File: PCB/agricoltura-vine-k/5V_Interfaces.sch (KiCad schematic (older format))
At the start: 26 parts, among them K1 G5LE-14_DC5, K2 G5LE-14_DC5, Q1 IRLML6346TRPBF, Q2 IRLML6346TRPBF, T19 TSW-108-07-G-T, T20 0010897080, T22 0395121006, U10 ZXGD3009E6TA, U8 TCA6416ARTWR, U9 ZXGD3009E6TA

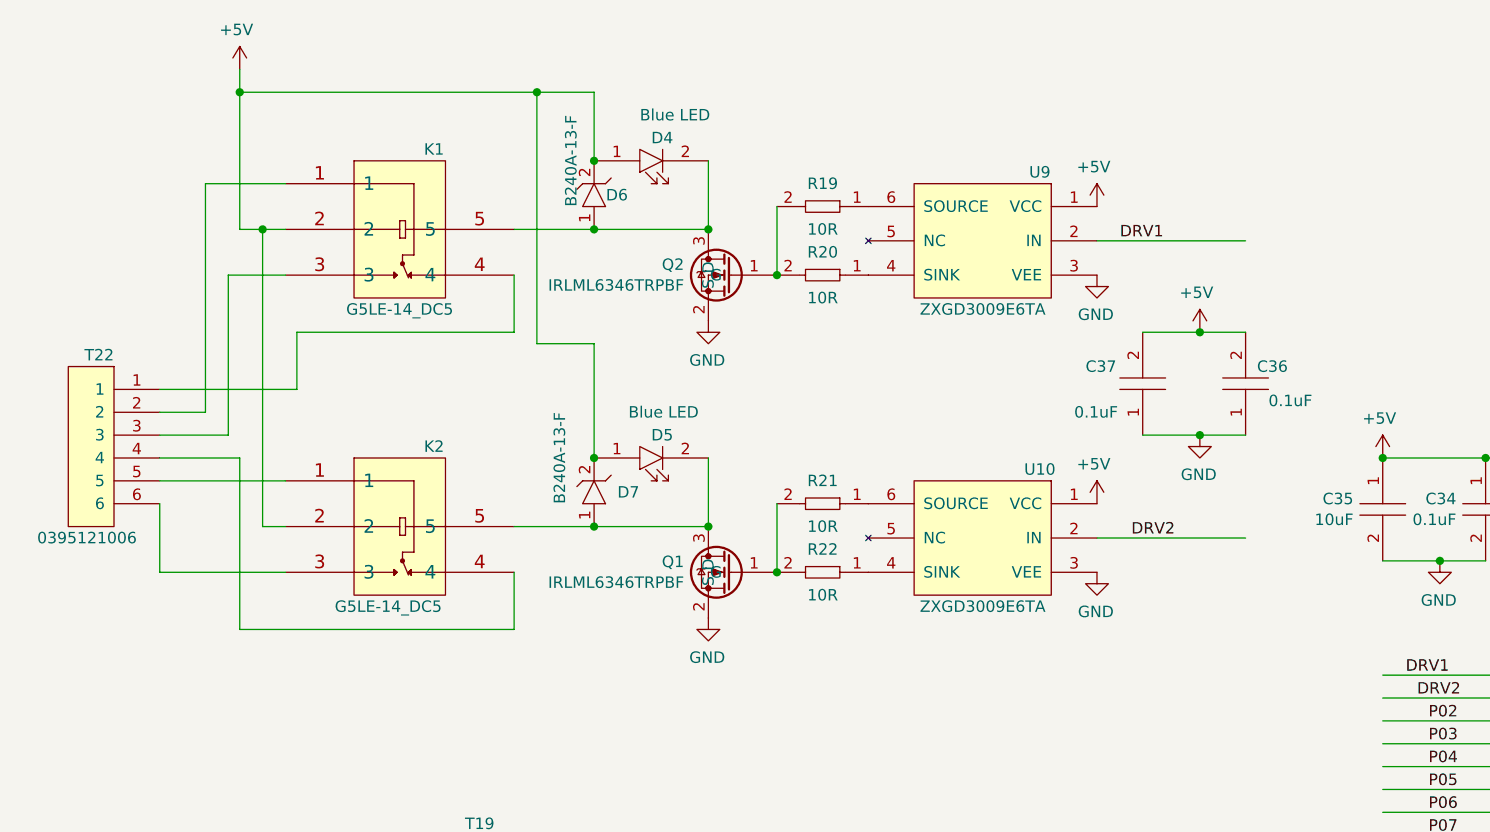
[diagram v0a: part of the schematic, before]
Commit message: Relay and Board
Relay circuits added and exported to PCB
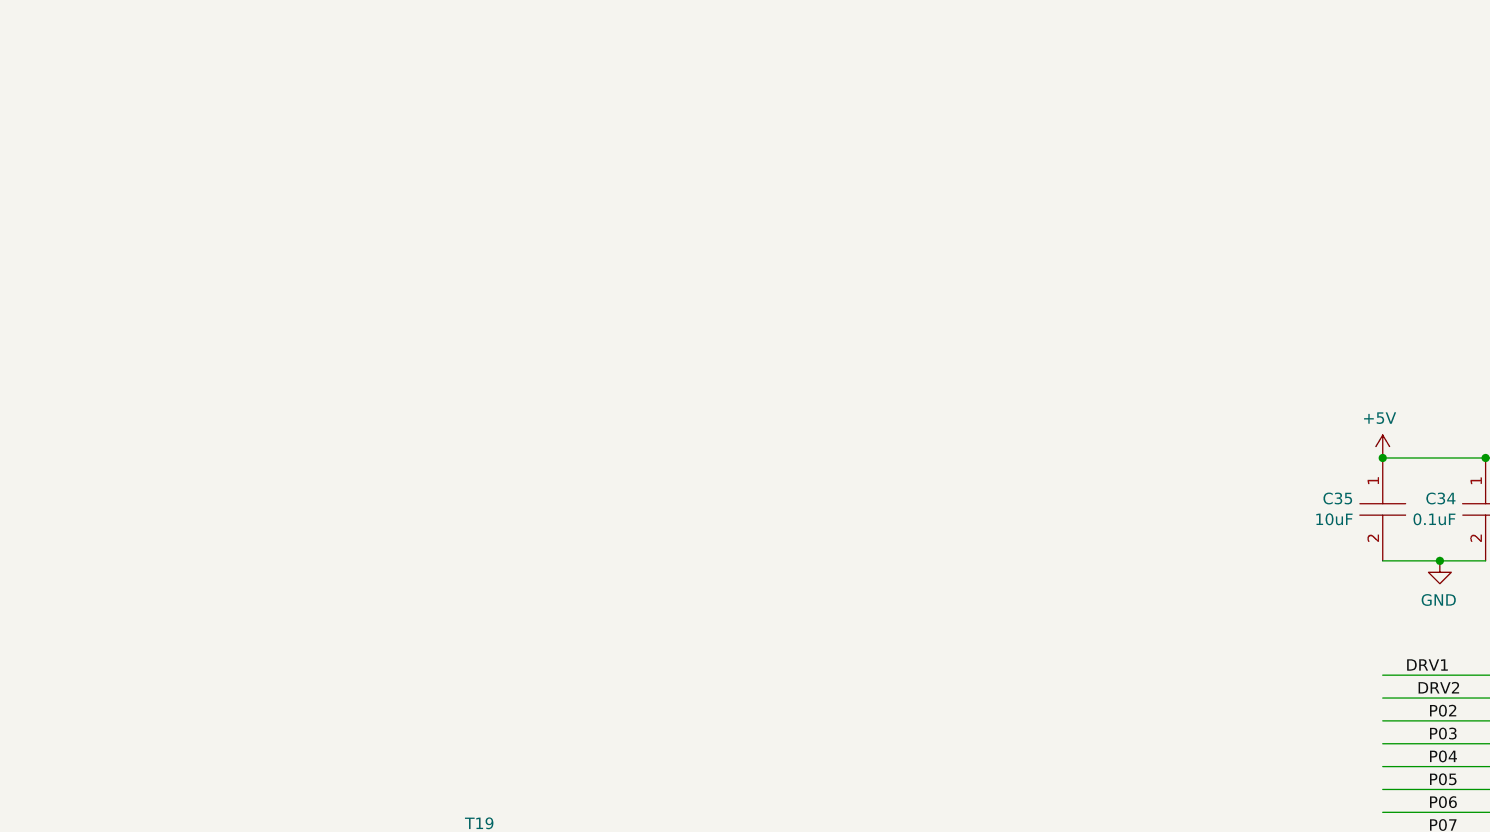
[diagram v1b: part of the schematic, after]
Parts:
- removed C36, C37: C0402C104K9PACTU, AVR-KiCAD-Lib-Resistors:R0402, symbol AVR-KiCAD-Lib-Capacitors:C0402C104K9PACTU
- removed D4, D5: LTST-C194TBKT, AVR-KiCAD-Lib-Diodes:LED0603, symbol AVR-KiCAD-Lib-Diodes:LTST-C194TBKT
- removed D6, D7: B240A-13-F, AVR-KiCAD-Lib-Diodes:B240A-13-F, symbol AVR-KiCAD-Lib-Diodes:B240A-13-F
- removed K1, K2: G5LE-14_DC5, AVR-KiCAD-Lib-Relays-Contactors:G5LE-14_DC5, symbol AVR-KiCAD-Lib-Mech-Relays-Contactors:G5LE-14_DC5
- removed Q1, Q2: IRLML6346TRPBF, AVR-KiCAD-Lib-Transistors:SOT-23, symbol AVR-KiCAD-Lib-Transistors:IRLML6346TRPBF
- removed R19, R20, R21, R22: RC0402FR-0710RL, AVR-KiCAD-Lib-Resistors:R0402, symbol AVR-KiCAD-Lib-Diodes:RC0402FR-0710RL
- removed T22: 0395121006, AVR-KiCAD-Lib-Connectors:0395121006, symbol AVR-KiCAD-Lib-Connectors:0395121006
- removed U10, U9: ZXGD3009E6TA, growbox-KiCAD-ICs:SOT-23-6_Handsoldering, symbol AVR-KiCAD-Lib-ICs:ZXGD3009E6TA
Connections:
- wire segments 106 -> 63

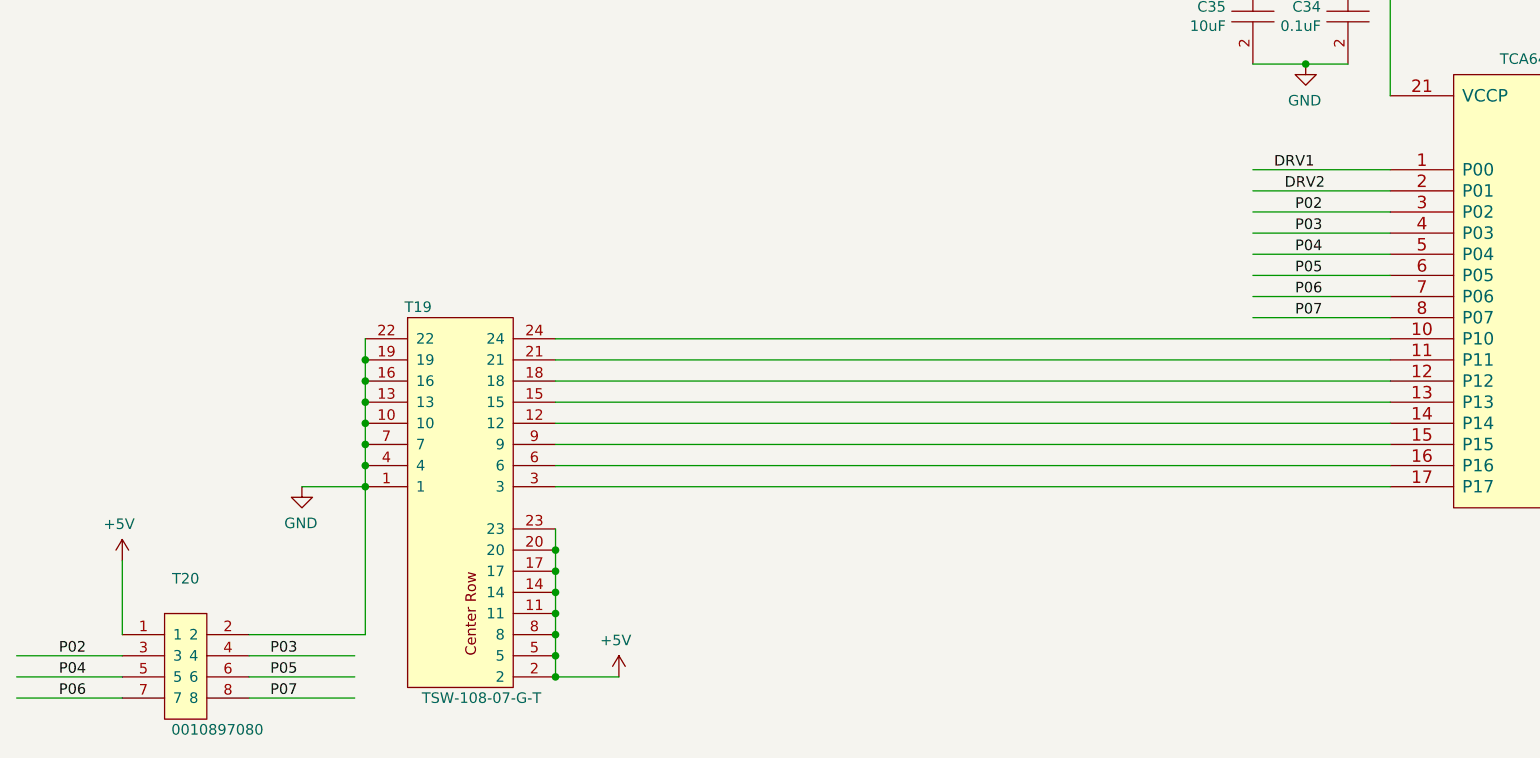
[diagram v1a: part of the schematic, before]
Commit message: Finished
PCB routing complete, up for review before fab.
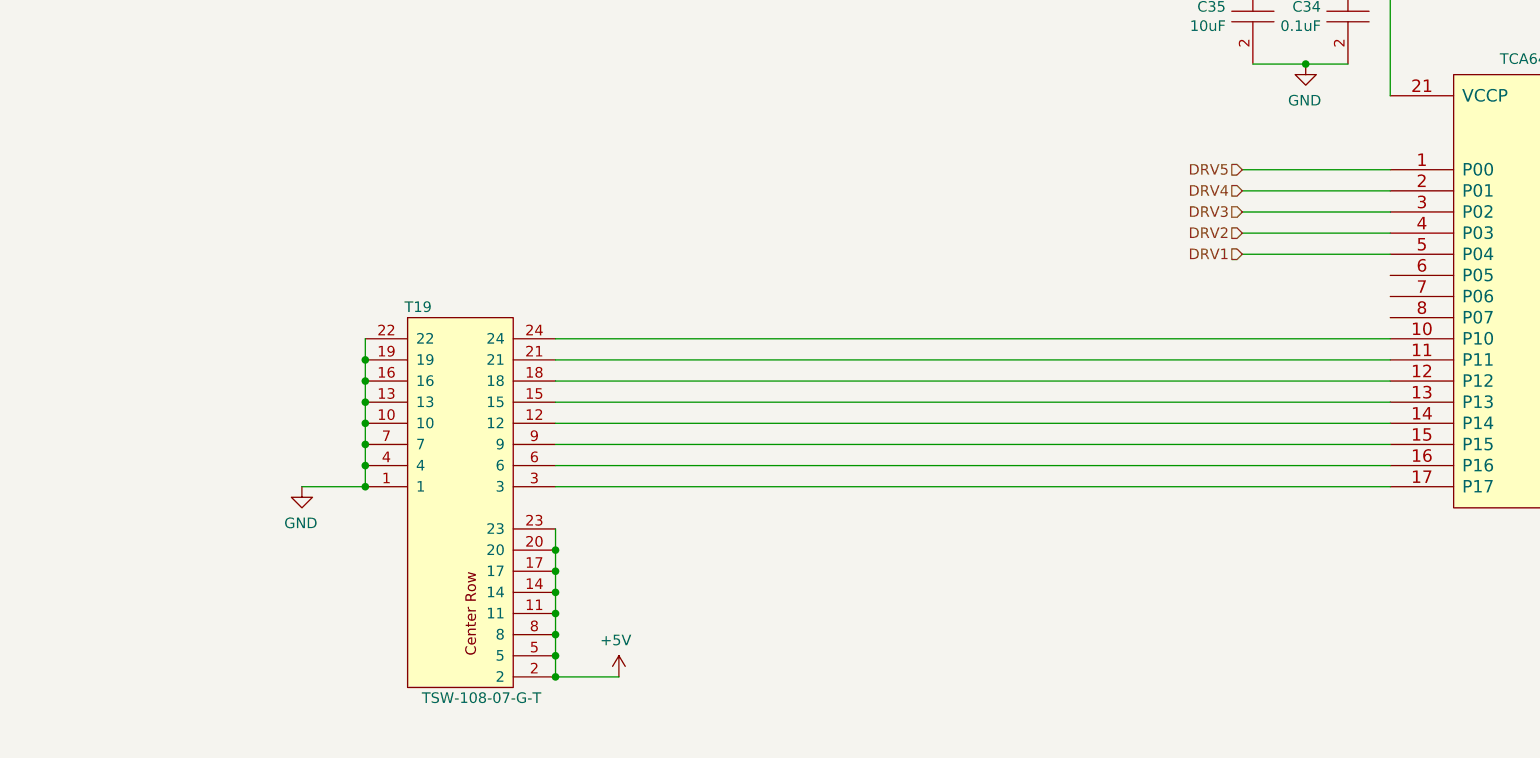
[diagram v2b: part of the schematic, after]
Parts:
- removed T20: 0010897080, AVR-KiCAD-Lib-Connectors:Pin_Header_Straight_2x04_Pitch2.54mm, symbol AVR-KiCAD-Lib-Connectors:0010897080
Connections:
- net labels added: DRV3, DRV4, DRV5
- net labels removed: P02, P03, P04, P05, P06, P07
- wire segments 63 -> 51
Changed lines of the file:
@@
 $EndDescr
-$Comp
-L AVR-KiCAD-Lib-Connectors:TSW-108-07-G-T T19
-U 1 1 5F0EF8CA
-P 2800 5200
-F 0 "T19" H 2850 5250 50  0000 C CNN
-F 1 "TSW-108-07-G-T" H 3150 3400 50  0000 C CNN
-F 2 "AVR-KiCAD-Lib-Connectors:TSW-108-07-G-T" H 2600 5200 50  0001 C CNN
-F 3 "http://suddendocs.samtec.com/catalog_english/tsw_th.pdf" H 2700 5300 50  0001 C CNN
-F 4 "2.51000" H 2900 5450 50  0001 C CNN "Cost QTY: 1"
-F 5 "1.39350" H 3000 5550 50  0001 C CNN "Cost QTY: 1000"
-F 6 "*" H 3100 5650 50  0001 C CNN "Cost QTY: 2500"
-F 7 "1.23557" H 3200 5750 50  0001 C CNN "Cost QTY: 5000"
-F 8 "1.20770" H 3300 5850 50  0001 C CNN "Cost QTY: 10000"
-F 9 "Samtec Inc." H 3400 5950 50  0001 C CNN "MFR"
-F 10 "TSW-108-07-G-T" H 3500 6050 50  0001 C CNN "MFR#"
-F 11 "Digikey" H 3600 6150 50  0001 C CNN "Vendor"
-F 12 "SAM10855-ND" H 3700 6250 50  0001 C CNN "Vendor #"
-F 13 "AVR" H 3800 6350 50  0001 C CNN "Designer"
-F 14 "10.92mm" H 3900 6450 50  0001 C CNN "Height"
-F 15 "6/18/2020" H 5000 7550 50  0001 C CNN "Date Created"
-F 16 "6/18/2020" H 4000 6550 50  0001 C CNN "Date Modified"
-F 17 "Yes" H 4100 6650 50  0001 C CNN "Lead-Free ?"
-F 18 "1" H 4200 6750 50  0001 C CNN "RoHS Levels"
-F 19 "SMT" H 4300 6850 50  0001 C CNN "Mounting"
-F 20 "24" H 4400 6950 50  0001 C CNN "Pin Count #"
-F 21 "Active" H 4500 7050 50  0001 C CNN "Status"
-F 22 "*" H 4600 7150 50  0001 C CNN "Tolerance"
-F 23 "Connector" H 4700 7250 50  0001 C CNN "Type"
-F 24 "*" H 4800 7350 50  0001 C CNN "Voltage"
-F 25 "*" H 4900 7500 50  0001 C CNN "Package"
-F 26 "Connector Header Through Hole 24 position 0.100\" (2.54mm)" H 5300 7900 50  0001 C CNN "Description"
-F 27 "3X08" H 5100 7700 50  0001 C CNN "_Value_"
-F 28 "*" H 5200 7800 50  0001 C CNN "Management_ID"
-	1    2800 5200
-	1    0    0    -1
-$EndComp
 $Comp
 L power:GND #PWR061
@@
 Connection ~ 10500 3900
 Wire Wire Line
+	7450 5300 3500 5300
+Wire Wire Line
+	7450 5400 3500 5400
+Wire Wire Line
+	7450 5500 3500 5500
+Wire Wire Line
+	7450 5600 3500 5600
+Wire Wire Line
+	7450 5700 3500 5700
+Wire Wire Line
+	7450 5800 3500 5800
+Wire Wire Line
+	7450 5900 3500 5900
+Wire Wire Line
+	7450 6000 3500 6000
+Connection ~ 10500 4700
+Connection ~ 10150 4800
+Wire Wire Line
+	10750 4700 10500 4700
+Wire Wire Line
+	10750 4800 10150 4800
+Connection ~ 7050 4000
+Text HLabel 6750 4600 0    50   Input ~ 0
+DRV4
+Text HLabel 6750 4700 0    50   Input ~ 0
+DRV3
+Text HLabel 6750 4800 0    50   Input ~ 0
+DRV2
+Text HLabel 6750 4900 0    50   Input ~ 0
+DRV1
+Text HLabel 6750 4500 0    50   Input ~ 0
+DRV5
+Connection ~ 2600 6000
+Connection ~ 3500 6700
+Connection ~ 2600 5800
+Wire Wire Line
+	3500 6700 3500 6800
+Wire Wire Line
+	3500 6800 3500 6900
+Connection ~ 3500 6800
+Wire Wire Line
+	2600 5900 2600 6000
+Wire Wire Line
+	2600 5800 2600 5900
+Connection ~ 2600 5900
+Wire Wire Line
 	3500 6200 3500 6300
-Wire Wire Line
-	7450 5300 3500 5300
-Wire Wire Line
-	7450 5400 3500 5400
-Wire Wire Line
-	7450 5500 3500 5500
-Wire Wire Line
-	7450 5600 3500 5600
-Wire Wire Line
-	7450 5700 3500 5700
-Wire Wire Line
-	7450 5800 3500 5800
-Wire Wire Line
-	7450 5900 3500 5900
-Wire Wire Line
-	7450 6000 3500 6000
+Connection ~ 3500 6300
 Connection ~ 3500 6900
-Connection ~ 3500 6800
-Wire Wire Line
-	3500 6800 3500 6900
-Connection ~ 3500 6700
-Wire Wire Line
-	3500 6700 3500 6800
-Connection ~ 3500 6600
-Wire Wire Line
-	3500 6600 3500 6700
+Wire Wire Line
+	2600 5300 2600 5400
+Connection ~ 2600 5400
+Wire Wire Line
+	3500 6300 3500 6400
+Connection ~ 3500 6400
+Wire Wire Line
+	2600 5400 2600 5500
+Connection ~ 2600 5500
+Wire Wire Line
+	3500 6400 3500 6500
 Connection ~ 3500 6500
-Wire Wire Line
-	3500 6500 3500 6600
-Connection ~ 3500 6400
-Wire Wire Line
-	3500 6400 3500 6500
-Connection ~ 3500 6300
-Wire Wire Line
-	3500 6300 3500 6400
-Wire Wire Line
-	2600 5300 2600 5400
-Wire Wire Line
-	2600 5400 2600 5500
-Connection ~ 2600 5400
-Connection ~ 2600 6000
-Connection ~ 2600 5500
 Wire Wire Line
 	2600 5500 2600 5600
 Connection ~ 2600 5600
 Wire Wire Line
+	3500 6500 3500 6600
+Wire Wire Line
+	3500 6600 3500 6700
+Connection ~ 3500 6600
+Wire Wire Line
+	2600 5700 2600 5800
+Wire Wire Line
 	2600 5600 2600 5700
 Connection ~ 2600 5700
-Wire Wire Line
-	2600 5700 2600 5800
-Connection ~ 2600 5800
-Wire Wire Line
-	2600 5800 2600 5900
-Connection ~ 2600 5900
-Wire Wire Line
-	2600 5900 2600 6000
-Connection ~ 10500 4700
-Connection ~ 10150 4800
-Wire Wire Line
-	10750 4700 10500 4700
-Wire Wire Line
-	10750 4800 10150 4800
-Connection ~ 7050 4000
-Wire Wire Line
-	6800 4500 7450 4500
-Text Label 6900 4500 0    50   ~ 0
-DRV1
-$Comp
-L AVR-KiCAD-Lib-Connectors:0010897080 T20
-U 1 1 5EFE35FE
-P 1650 6600
-F 0 "T20" H 1750 6765 50  0000 C CNN
-F 1 "0010897080" H 1900 6050 50  0000 C CNN
-F 2 "AVR-KiCAD-Lib-Connectors:Pin_Header_Straight_2x04_Pitch2.54mm" H 1450 6550 50  0001 C CNN
-F 3 "https://www.molex.com/pdm_docs/sd/010897080_sd.pdf" H 1550 6700 50  0001 C CNN
-F 4 "1.05000" H 1750 6850 50  0001 C CNN "Cost QTY: 1"
-F 5 "0.57952" H 1850 6950 50  0001 C CNN "Cost QTY: 1000"
-F 6 "*" H 1950 7050 50  0001 C CNN "Cost QTY: 2500"
-F 7 "0.50708" H 2050 7150 50  0001 C CNN "Cost QTY: 5000"
-F 8 "0.48173" H 2150 7250 50  0001 C CNN "Cost QTY: 10000"
-F 9 "Molex" H 2250 7350 50  0001 C CNN "MFR"
-F 10 "0010897080" H 2350 7450 50  0001 C CNN "MFR#"
-F 11 "Digikey" H 2450 7550 50  0001 C CNN "Vendor"
-F 12 "0010897080" H 2550 7650 50  0001 C CNN "Vendor #"
-F 13 "AVR" H 2650 7750 50  0001 C CNN "Designer"
-F 14 "8.4mm" H 2750 7850 50  0001 C CNN "Height"
-F 15 "6/30/2020" H 3850 8950 50  0001 C CNN "Date Created"
-F 16 "6/30/2020" H 2850 7950 50  0001 C CNN "Date Modified"
-F 17 "Yes" H 2950 8050 50  0001 C CNN "Lead-Free ?"
-F 18 "1" H 3050 8150 50  0001 C CNN "RoHS Levels"
-F 19 "ThroughHole" H 3150 8250 50  0001 C CNN "Mounting"
-F 20 "8" H 3250 8350 50  0001 C CNN "Pin Count #"
-F 21 "Active" H 3350 8450 50  0001 C CNN "Status"
-F 22 "*" H 3450 8550 50  0001 C CNN "Tolerance"
-F 23 "Pin Header" H 3550 8650 50  0001 C CNN "Type"
-F 24 "*" H 3650 8750 50  0001 C CNN "Voltage"
-F 25 "*" H 3750 8900 50  0001 C CNN "Package"
-F 26 "Connector Header Through Hole 8 position 0.100\" (2.54mm)" H 4150 9300 50  0001 C CNN "Description"
-F 27 "2X04" H 3950 9100 50  0001 C CNN "_Value_"
-F 28 "*" H 4050 9200 50  0001 C CNN "Management_ID"
-	1    1650 6600
+$Comp
+L AVR-KiCAD-Lib-Connectors:TSW-108-07-G-T T19
+U 1 1 5F0EF8CA
+P 2800 5200
+F 0 "T19" H 2850 5250 50  0000 C CNN
+F 1 "TSW-108-07-G-T" H 3150 3400 50  0000 C CNN
+F 2 "AVR-KiCAD-Lib-Connectors:TSW-108-07-G-T" H 2600 5200 50  0001 C CNN
+F 3 "http://suddendocs.samtec.com/catalog_english/tsw_th.pdf" H 2700 5300 50  0001 C CNN
+F 4 "2.51000" H 2900 5450 50  0001 C CNN "Cost QTY: 1"
+F 5 "1.39350" H 3000 5550 50  0001 C CNN "Cost QTY: 1000"
+F 6 "*" H 3100 5650 50  0001 C CNN "Cost QTY: 2500"
+F 7 "1.23557" H 3200 5750 50  0001 C CNN "Cost QTY: 5000"
+F 8 "1.20770" H 3300 5850 50  0001 C CNN "Cost QTY: 10000"
+F 9 "Samtec Inc." H 3400 5950 50  0001 C CNN "MFR"
+F 10 "TSW-108-07-G-T" H 3500 6050 50  0001 C CNN "MFR#"
+F 11 "Digikey" H 3600 6150 50  0001 C CNN "Vendor"
+F 12 "SAM10855-ND" H 3700 6250 50  0001 C CNN "Vendor #"
+F 13 "AVR" H 3800 6350 50  0001 C CNN "Designer"
+F 14 "10.92mm" H 3900 6450 50  0001 C CNN "Height"
+F 15 "6/18/2020" H 5000 7550 50  0001 C CNN "Date Created"
+F 16 "6/18/2020" H 4000 6550 50  0001 C CNN "Date Modified"
+F 17 "Yes" H 4100 6650 50  0001 C CNN "Lead-Free ?"
+F 18 "1" H 4200 6750 50  0001 C CNN "RoHS Levels"
+F 19 "SMT" H 4300 6850 50  0001 C CNN "Mounting"
+F 20 "24" H 4400 6950 50  0001 C CNN "Pin Count #"
+F 21 "Active" H 4500 7050 50  0001 C CNN "Status"
+F 22 "*" H 4600 7150 50  0001 C CNN "Tolerance"
+F 23 "Connector" H 4700 7250 50  0001 C CNN "Type"
+F 24 "*" H 4800 7350 50  0001 C CNN "Voltage"
+F 25 "*" H 4900 7500 50  0001 C CNN "Package"
+F 26 "Connector Header Through Hole 24 position 0.100\" (2.54mm)" H 5300 7900 50  0001 C CNN "Description"
+F 27 "3X08" H 5100 7700 50  0001 C CNN "_Value_"
+F 28 "*" H 5200 7800 50  0001 C CNN "Management_ID"
+	1    2800 5200
 	1    0    0    -1
 $EndComp
-$Comp
-L power:+5V #PWR0128
-U 1 1 5F003EA5
-P 1450 6350
-F 0 "#PWR0128" H 1450 6200 50  0001 C CNN
-F 1 "+5V" H 1465 6523 50  0000 C CNN
-F 2 "" H 1450 6350 50  0001 C CNN
-F 3 "" H 1450 6350 50  0001 C CNN
-	1    1450 6350
-	-1   0    0    -1
-$EndComp
-Wire Wire Line
-	1450 6700 1450 6350
-Wire Wire Line
-	2050 6700 2600 6700
-Text Label 6950 4600 0    50   ~ 0
-DRV2
-Wire Wire Line
-	6800 4600 7450 4600
-Wire Wire Line
-	1450 6800 950  6800
-Wire Wire Line
-	1450 6900 950  6900
-Wire Wire Line
-	1450 7000 950  7000
-Wire Wire Line
-	2550 6800 2050 6800
-Wire Wire Line
-	2550 6900 2050 6900
-Wire Wire Line
-	2550 7000 2050 7000
-Text Label 1150 6800 0    50   ~ 0
-P02
-Text Label 7000 4700 0    50   ~ 0
-P02
-Wire Wire Line
-	6800 4700 7450 4700
-Wire Wire Line
-	6800 4800 7450 4800
-Wire Wire Line
-	6800 4900 7450 4900
-Wire Wire Line
-	6800 5000 7450 5000
-Wire Wire Line
-	6800 5100 7450 5100
-Wire Wire Line
-	6800 5200 7450 5200
-Text Label 2150 6800 0    50   ~ 0
-P03
-Text Label 7000 4800 0    50   ~ 0
-P03
-Text Label 1150 6900 0    50   ~ 0
-P04
-Text Label 7000 4900 0    50   ~ 0
-P04
-Text Label 2150 6900 0    50   ~ 0
-P05
-Text Label 1150 7000 0    50   ~ 0
-P06
-Text Label 2150 7000 0    50   ~ 0
-P07
-Text Label 7000 5000 0    50   ~ 0
-P05
-Text Label 7000 5100 0    50   ~ 0
-P06
-Text Label 7000 5200 0    50   ~ 0
-P07
-Wire Wire Line
-	2600 6000 2600 6700
+Wire Wire Line
+	6750 4500 7450 4500
+Wire Wire Line
+	7450 4600 6750 4600
+Wire Wire Line
+	7450 4700 6750 4700
+Wire Wire Line
+	7450 4800 6750 4800
+Wire Wire Line
+	7450 4900 6750 4900
 $EndSCHEMATC
